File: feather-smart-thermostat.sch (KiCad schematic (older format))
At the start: 6 parts, among them SW1 Temp Up, SW2 Temp Down, SW3 Function, U1 SHT31-D, U2 FeatherHuzzahBoard

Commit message: have an example code that works
Also customize the driver to reduce the update time to 1s instead of the amount it was taking before
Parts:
- RELAY?: symbol components:SingleRelayModuleD25 -> feather-smart-thermostat-rescue:SingleRelayModuleD25-components
- U1: symbol Adafruit_SHT31_Breakout-eagle-import:SHT3X -> feather-smart-thermostat-rescue:SHT3X-Adafruit_SHT31_Breakout-eagle-import
- U2: symbol components:FeatherHuzzahBoard -> feather-smart-thermostat-rescue:FeatherHuzzahBoard-components
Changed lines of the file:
@@
 	2650 2950 2750 3050
 $Comp
-L Adafruit_SHT31_Breakout-eagle-import:SHT3X U1
+L feather-smart-thermostat-rescue:SHT3X-Adafruit_SHT31_Breakout-eagle-import U1
 U 1 1 5F8F5E69
 P 5550 2950
@@
 $EndComp
 $Comp
-L components:FeatherHuzzahBoard U2
+L feather-smart-thermostat-rescue:FeatherHuzzahBoard-components U2
 U 1 1 5F905B59
 P 4700 4800
@@
 	7100 1750 4000 1750
 $Comp
-L components:SingleRelayModuleD25 RELAY?
+L feather-smart-thermostat-rescue:SingleRelayModuleD25-components RELAY?
 U 1 1 5F91202D
 P 6050 6700
@@
 Wire Wire Line
 	6800 3900 6250 3900
+Entry Wire Line
+	8750 6000 8850 6100
+Entry Wire Line
+	2650 6050 2750 6150
 Wire Bus Line
 	8850 1700 8850 6700
 Wire Bus Line
 	2650 1850 2650 6500
-Entry Wire Line
-	8750 6000 8850 6100
-Entry Wire Line
-	2650 6050 2750 6150
 $EndSCHEMATC

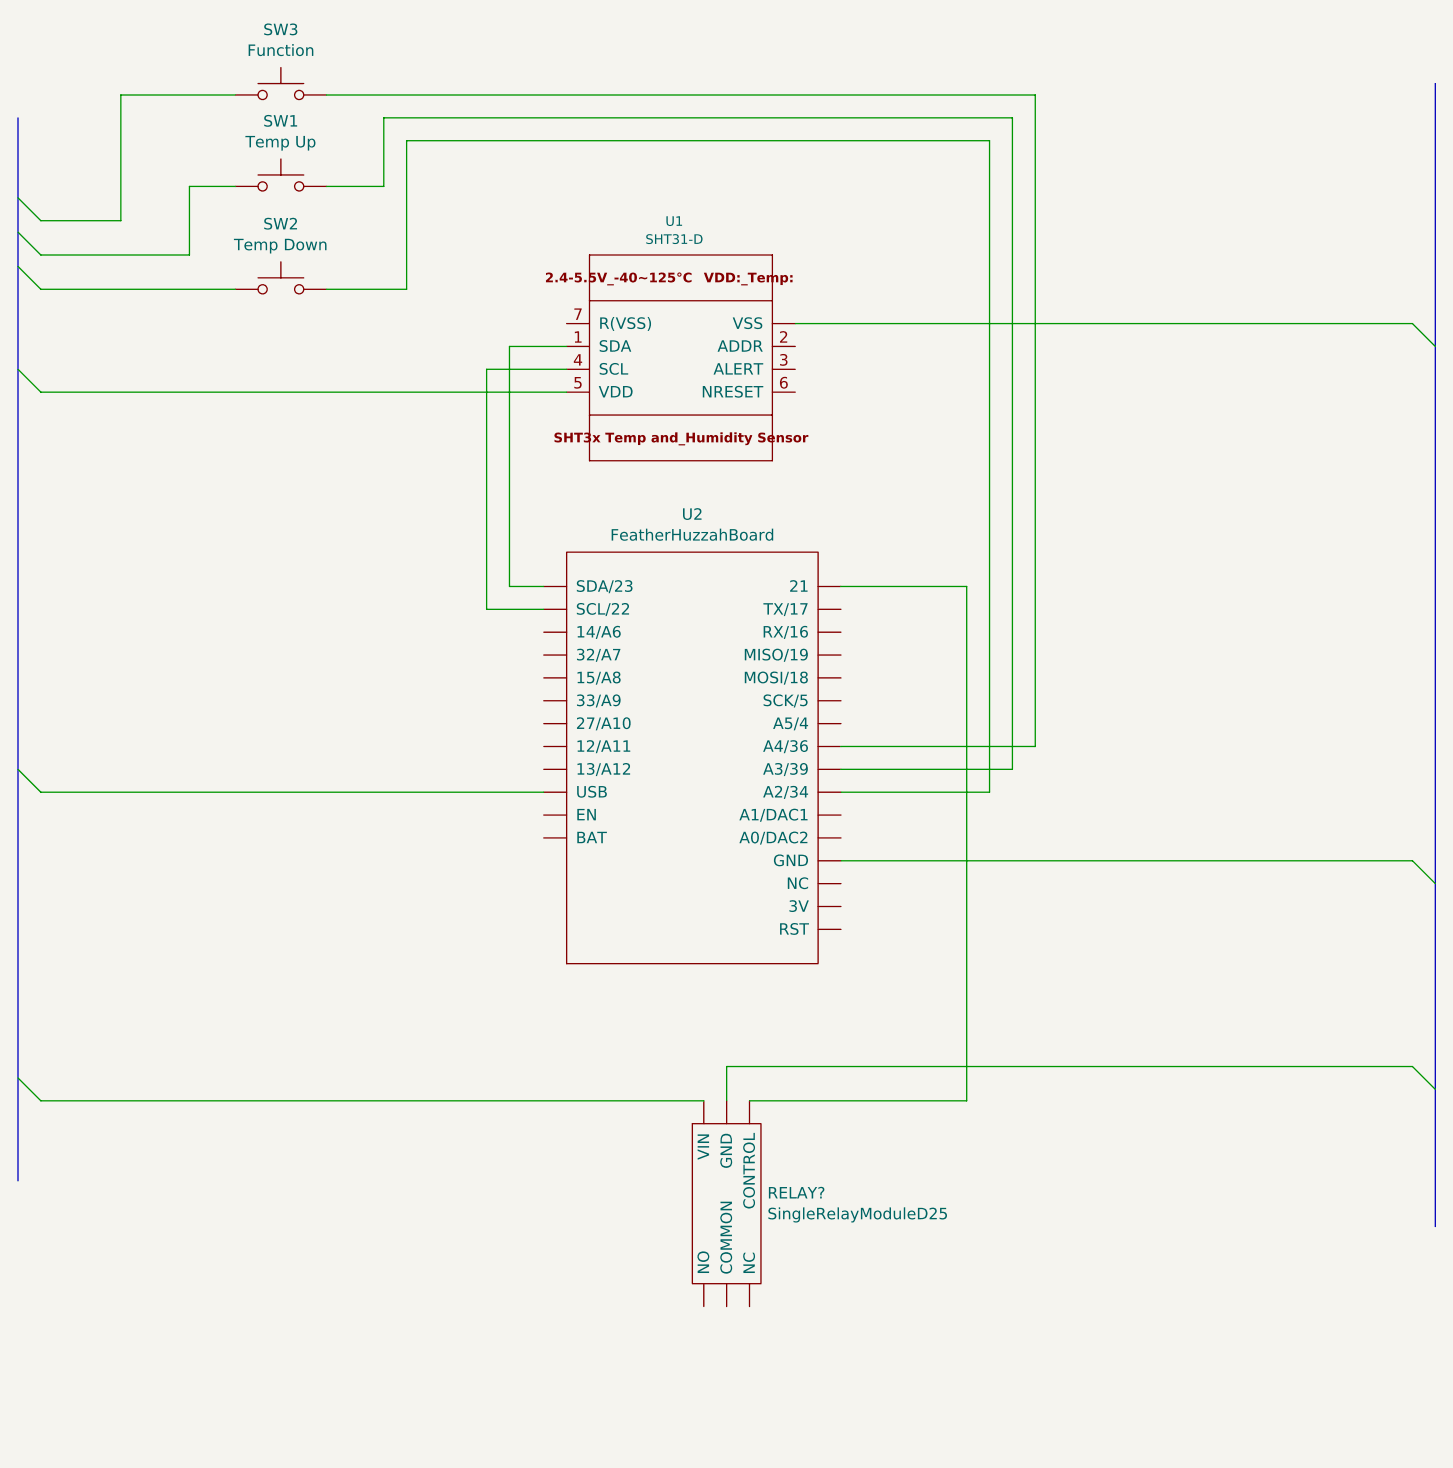
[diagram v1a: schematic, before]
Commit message: use the current sensor
Also change some pins since we cannot use ADC2
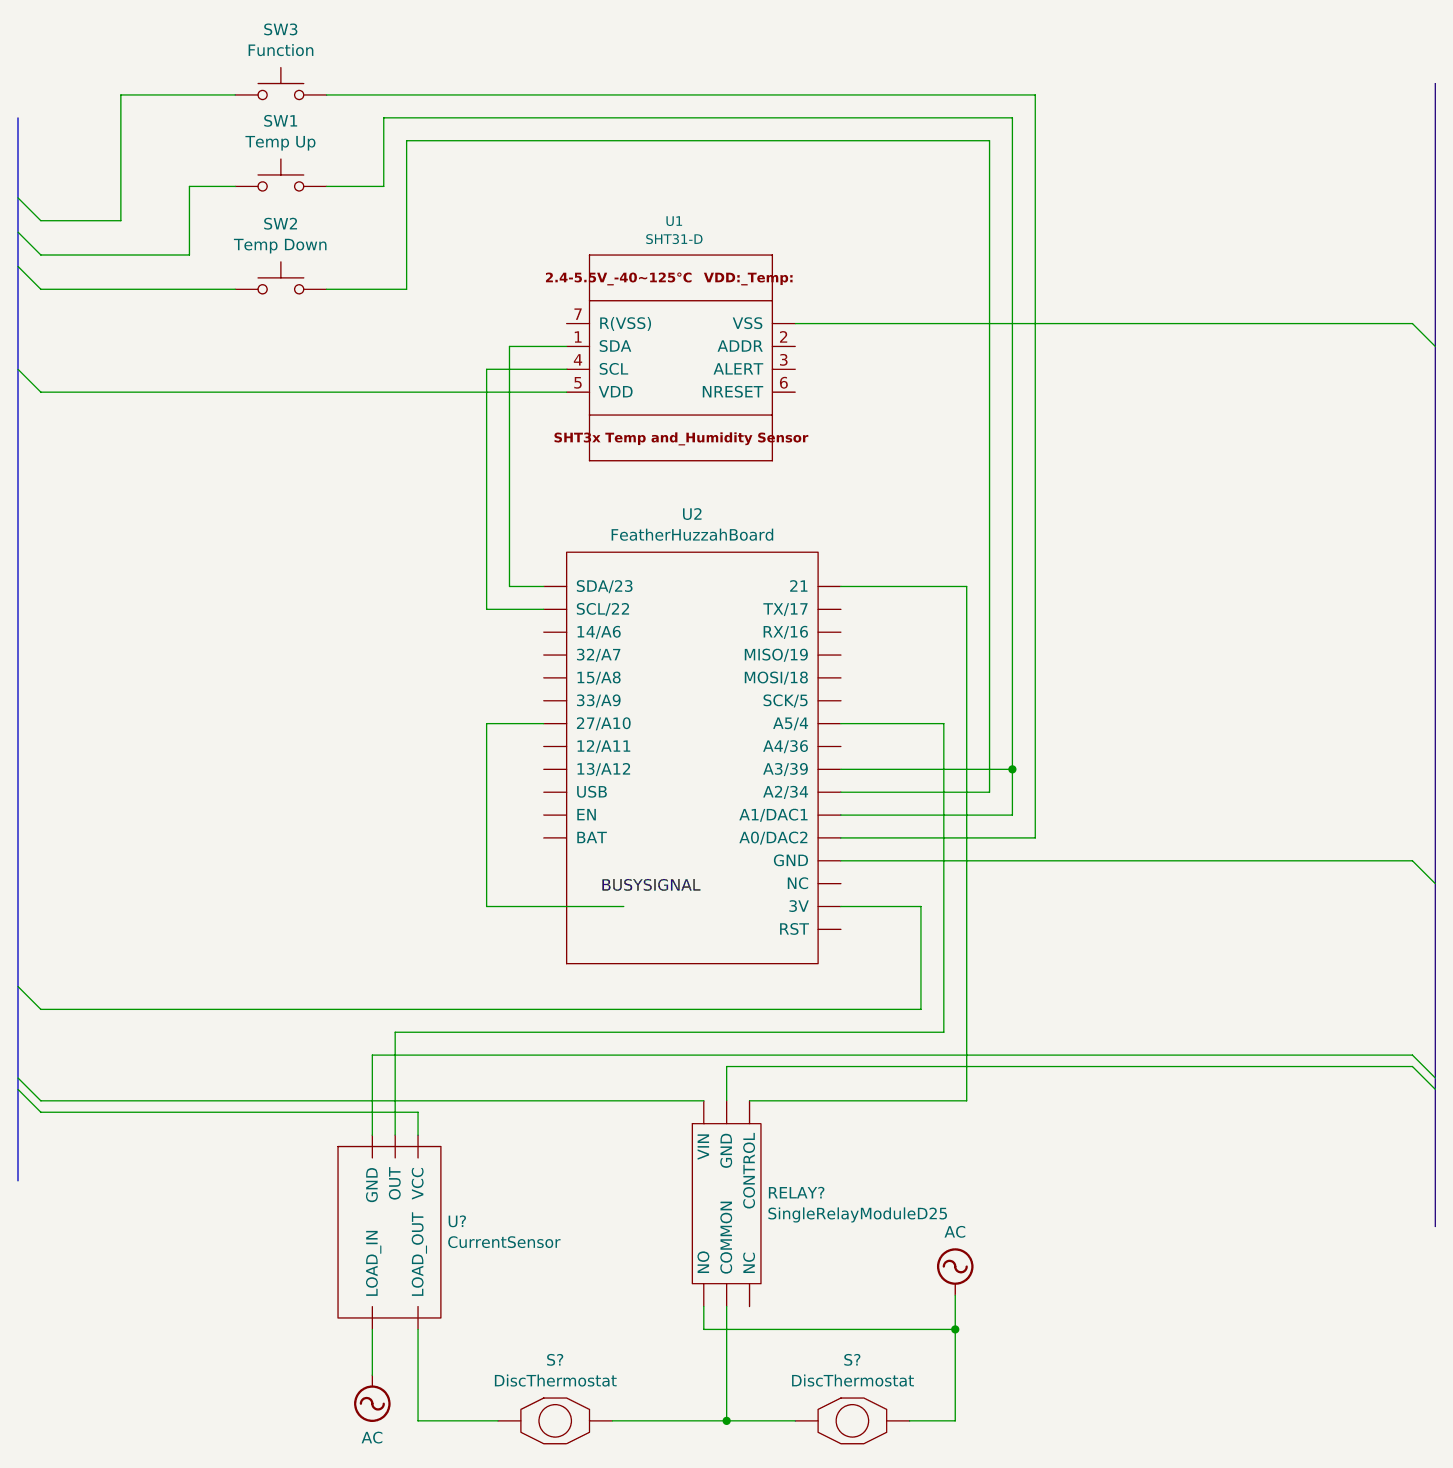
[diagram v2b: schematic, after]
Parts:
- added S? (x2): DiscThermostat, symbol feather-smart-thermostat-rescue:DiscThermostat
- added U?: CurrentSensor, symbol feather-smart-thermostat-rescue:CurrentSensor
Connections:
- net at U2.~ (USB): now also RELAY?.~ (VIN)
- net AC: now reaches RELAY?.~ (VIN)
- net AC: now also S?.~, U?.~ (VCC); no longer U2.~ (USB)
- new net: S?.~, U?.~ (VCC)
- new net: U2.~ (USB), U?.~ (VCC)
- new net: RELAY?.~ (VIN), S?.~, S?.~
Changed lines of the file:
@@
 EESchema Schematic File Version 4
-EELAYER 30 0
+LIBS:feather-smart-thermostat-cache
+EELAYER 26 0
 EELAYER END
 $Descr A4 11693 8268
@@
 $EndComp
 Wire Wire Line
-	4950 4800 2750 4800
-Entry Wire Line
-	2650 4700 2750 4800
-Wire Wire Line
 	6250 5100 8750 5100
 Entry Wire Line
@@
 	4350 2600 4000 2600
 Wire Wire Line
-	6250 4700 7000 4700
-Wire Wire Line
-	7000 4700 7000 1850
-Wire Wire Line
 	7000 1850 4250 1850
 Wire Wire Line
@@
 Wire Wire Line
 	4250 2150 4000 2150
-Wire Wire Line
-	6250 4600 7100 4600
-Wire Wire Line
-	7100 4600 7100 1750
 Wire Wire Line
 	7100 1750 4000 1750
@@
 Entry Wire Line
 	2650 6050 2750 6150
+Text Label 5200 5250 0    50   ~ 0
+BUSYSIGNAL
+Wire Wire Line
+	5300 5300 4700 5300
+Wire Wire Line
+	4700 5300 4700 4500
+Wire Wire Line
+	4700 4500 4950 4500
+$Comp
+L feather-smart-thermostat-rescue:CurrentSensor U?
+U 1 1 5F8B457D
+P 4400 5150
+F 0 "U?" H 4528 3621 50  0000 L CNN
+F 1 "CurrentSensor" H 4528 3530 50  0000 L CNN
+F 2 "" H 4400 5150 50  0001 C CNN
+F 3 "" H 4400 5150 50  0001 C CNN
+	1    4400 5150
+	1    0    0    -1
+$EndComp
+Wire Wire Line
+	4200 6300 4200 5950
+Wire Wire Line
+	4200 5950 8750 5950
+Wire Wire Line
+	4400 6300 4400 6200
+Wire Wire Line
+	4400 6200 2750 6200
+Wire Wire Line
+	4300 6300 4300 5850
+Wire Wire Line
+	4300 5850 6700 5850
+Wire Wire Line
+	6700 5850 6700 4500
+Wire Wire Line
+	6700 4500 6250 4500
+$Comp
+L power:AC #PWR?
+U 1 1 5F8B7DE8
+P 4200 7350
+F 0 "#PWR?" H 4200 7250 50  0001 C CNN
+F 1 "AC" H 4200 7625 50  0000 C CNN
+F 2 "" H 4200 7350 50  0001 C CNN
+F 3 "" H 4200 7350 50  0001 C CNN
+	1    4200 7350
+	-1   0    0    1
+$EndComp
+Wire Wire Line
+	4200 7350 4200 7150
+$Comp
+L feather-smart-thermostat-rescue:DiscThermostat S?
+U 1 1 5F8B995B
+P 5000 7400
+F 0 "S?" H 5000 7515 50  0000 C CNN
+F 1 "DiscThermostat" H 5000 7424 50  0000 C CNN
+F 2 "" H 5000 7400 50  0001 C CNN
+F 3 "" H 5000 7400 50  0001 C CNN
+	1    5000 7400
+	1    0    0    -1
+$EndComp
+$Comp
+L feather-smart-thermostat-rescue:DiscThermostat S?
+U 1 1 5F8B99FD
+P 6300 7400
+F 0 "S?" H 6300 7515 50  0000 C CNN
+F 1 "DiscThermostat" H 6300 7424 50  0000 C CNN
+F 2 "" H 6300 7400 50  0001 C CNN
+F 3 "" H 6300 7400 50  0001 C CNN
+	1    6300 7400
+	1    0    0    -1
+$EndComp
+Wire Wire Line
+	4400 7550 4750 7550
+Wire Wire Line
+	5250 7550 5750 7550
+Wire Wire Line
+	5750 7550 6050 7550
+Connection ~ 5750 7550
+Wire Wire Line
+	5650 7050 5650 7150
+Wire Wire Line
+	5650 7150 6750 7150
+Wire Wire Line
+	6750 7550 6550 7550
+Wire Wire Line
+	4400 7150 4400 7550
+Wire Wire Line
+	5750 7050 5750 7550
+Wire Wire Line
+	6750 7150 6750 7550
+Connection ~ 6750 7150
+Wire Wire Line
+	6750 7000 6750 7150
+$Comp
+L power:AC #PWR?
+U 1 1 5F8C2BAA
+P 6750 7000
+F 0 "#PWR?" H 6750 6900 50  0001 C CNN
+F 1 "AC" H 6750 7275 50  0000 C CNN
+F 2 "" H 6750 7000 50  0001 C CNN
+F 3 "" H 6750 7000 50  0001 C CNN
+	1    6750 7000
+	1    0    0    -1
+$EndComp
+Entry Wire Line
+	8750 5950 8850 6050
+Entry Wire Line
+	2650 6100 2750 6200
+Wire Wire Line
+	6250 5300 6600 5300
+Wire Wire Line
+	6600 5300 6600 5750
+Entry Wire Line
+	2650 5650 2750 5750
+Wire Wire Line
+	2750 5750 6600 5750
+Wire Wire Line
+	7000 4700 7000 1850
+Wire Wire Line
+	6250 4700 7000 4700
+Wire Wire Line
+	7100 5000 6250 5000
+Wire Wire Line
+	7000 4700 7000 4900
+Wire Wire Line
+	7000 4900 6250 4900
 Wire Bus Line
 	8850 1700 8850 6700
 Wire Bus Line
 	2650 1850 2650 6500
+Connection ~ 7000 4700
+Wire Wire Line
+	7100 1750 7100 5000
 $EndSCHEMATC

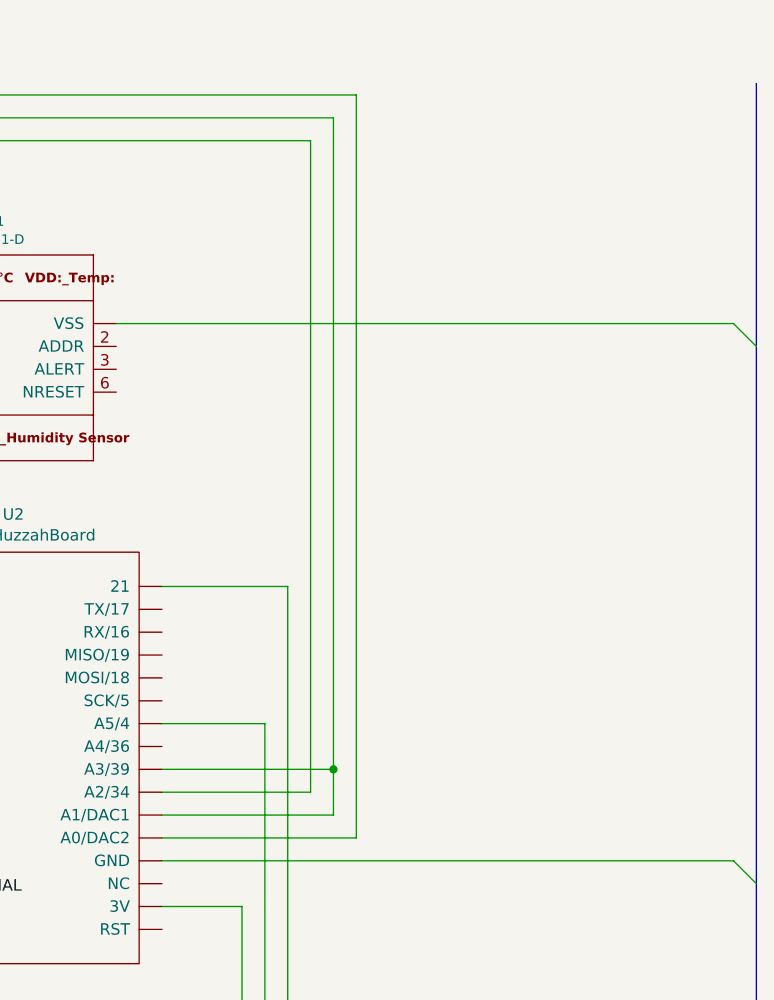
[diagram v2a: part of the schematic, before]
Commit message: finished cover, fixed obvious problem by grounding digital pins
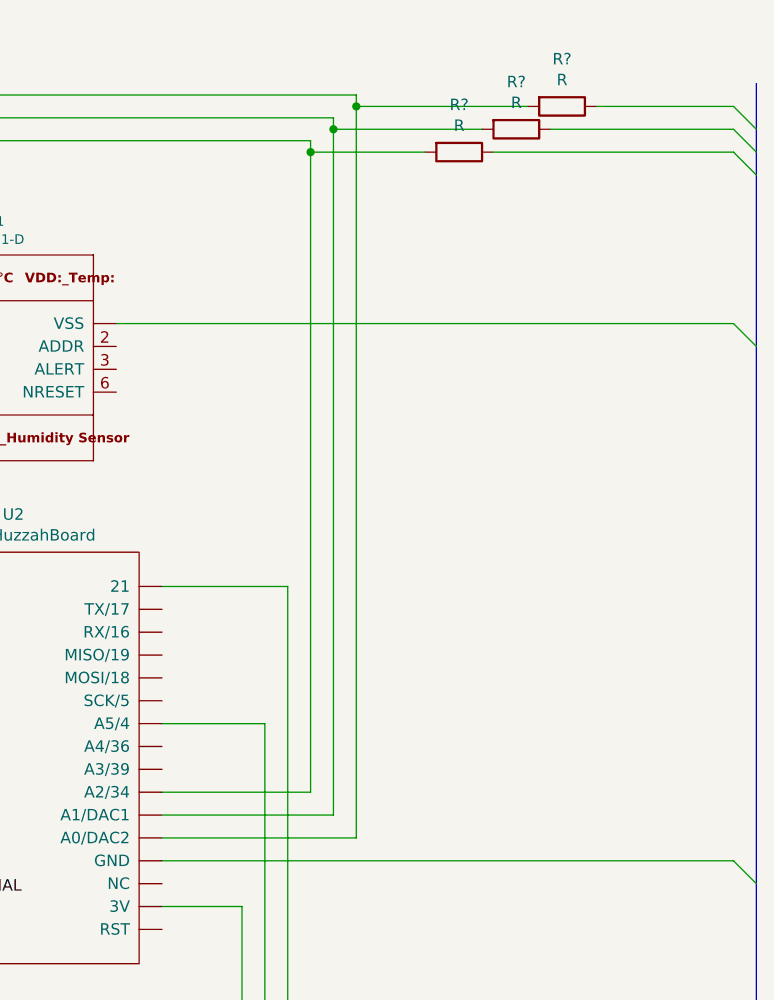
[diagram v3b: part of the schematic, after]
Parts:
- added R? (x3): R, symbol Device:R
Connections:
- net at S?.~: now also RELAY?.~ (VIN), S?.~; no longer U?.~ (VCC)
- net at U2.~ (USB): now also RELAY?.~ (VIN); no longer U?.~ (VCC)
- net at SW2.2, U2.~ (USB): now also R?.2
- net at SW1.2, U2.~ (USB): now also R?.2
- net at SW3.2, U2.~ (USB): now also R?.2
- new net: S?.~, U?.~ (VCC)
- new net: U2.~ (USB), U?.~ (VCC)
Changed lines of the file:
@@
 	6250 4800 6900 4800
 Wire Wire Line
-	6900 4800 6900 1950
+	6900 4800 6900 2000
 Wire Wire Line
 	6900 1950 4350 1950
@@
 	2750 5750 6600 5750
 Wire Wire Line
-	7000 4700 7000 1850
-Wire Wire Line
-	6250 4700 7000 4700
-Wire Wire Line
 	7100 5000 6250 5000
 Wire Wire Line
-	7000 4700 7000 4900
-Wire Wire Line
 	7000 4900 6250 4900
+Wire Wire Line
+	7100 1750 7100 1800
+Wire Wire Line
+	7000 1850 7000 1900
+$Comp
+L Device:R R?
+U 1 1 5FA950D5
+P 8000 1800
+F 0 "R?" V 7793 1800 50  0000 C CNN
+F 1 "R" V 7884 1800 50  0000 C CNN
+F 2 "" V 7930 1800 50  0001 C CNN
+F 3 "~" H 8000 1800 50  0001 C CNN
+	1    8000 1800
+	0    1    1    0
+$EndComp
+$Comp
+L Device:R R?
+U 1 1 5FA95194
+P 7800 1900
+F 0 "R?" V 7593 1900 50  0000 C CNN
+F 1 "R" V 7684 1900 50  0000 C CNN
+F 2 "" V 7730 1900 50  0001 C CNN
+F 3 "~" H 7800 1900 50  0001 C CNN
+	1    7800 1900
+	0    1    1    0
+$EndComp
+$Comp
+L Device:R R?
+U 1 1 5FA9524D
+P 7550 2000
+F 0 "R?" V 7343 2000 50  0000 C CNN
+F 1 "R" V 7434 2000 50  0000 C CNN
+F 2 "" V 7480 2000 50  0001 C CNN
+F 3 "~" H 7550 2000 50  0001 C CNN
+	1    7550 2000
+	0    1    1    0
+$EndComp
+Wire Wire Line
+	7700 2000 8750 2000
+Wire Wire Line
+	7100 1800 7850 1800
+Connection ~ 7100 1800
+Wire Wire Line
+	8150 1800 8750 1800
+Wire Wire Line
+	7950 1900 8750 1900
+Entry Wire Line
+	8750 1800 8850 1900
+Entry Wire Line
+	8750 1900 8850 2000
+Entry Wire Line
+	8750 2000 8850 2100
+Wire Wire Line
+	7100 1800 7100 5000
+Wire Wire Line
+	7650 1900 7000 1900
+Connection ~ 7000 1900
+Wire Wire Line
+	7000 1900 7000 4900
+Wire Wire Line
+	7400 2000 6900 2000
+Wire Bus Line
+	2650 1850 2650 6500
 Wire Bus Line
 	8850 1700 8850 6700
-Wire Bus Line
-	2650 1850 2650 6500
-Connection ~ 7000 4700
-Wire Wire Line
-	7100 1750 7100 5000
+Connection ~ 6900 2000
+Wire Wire Line
+	6900 2000 6900 1950
 $EndSCHEMATC
